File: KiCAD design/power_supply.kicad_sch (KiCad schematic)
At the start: 0 parts

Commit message: finished conectors / sensors / converters
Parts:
- added C? (x2): 1uF, Capacitor_SMD:C_0603_1608Metric_Pad1.08x0.95mm_HandSolder, symbol Device:C_Small
- added C?: 10uF, Capacitor_SMD:C_0603_1608Metric_Pad1.08x0.95mm_HandSolder, symbol Device:C_Small
- added C?: 22uF, Capacitor_SMD:C_0603_1608Metric_Pad1.08x0.95mm_HandSolder, symbol Device:C_Small
- added SW?: ~, composants_projet_footprint:1A11-NF5STSE-B, symbol Switch:SW_SPDT
- added U?: MIC5317, Package_TO_SOT_SMD:SOT-23-5, symbol Regulator_Linear:MCP1802x-xx02xOT
- added U?: A71117CH2-5.0TRG1, Package_TO_SOT_SMD:SOT-223-3_TabPin2, symbol Regulator_Linear:MCP1804x-1802xDB
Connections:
- new net +3V3: C?.1, U?.5 (VOUT)
- new net +5V: C?.1, C?.1, U?.1 (OUT), U?.1 (VIN), U?.3 (~{SHDN})
- new net +7.2V: C?.1, SW?.1 (A), U?.3 (IN)
- new net +BATT: SW?.2 (B)
- new net GND: C?.2, C?.2, C?.2, C?.2, U?.2 (GND), U?.2 (GND)
- no-connect marks 0 -> 1
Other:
- note added: "3.3V Power supply"
- note added: "5V Power supply"
- note added: "Bypass capacitor as close to the LDO (pin 1 VIN) as possible"
- note added: "SWITCH"
- company: (none) -> Oulu University
- title: (none) -> Power Supply

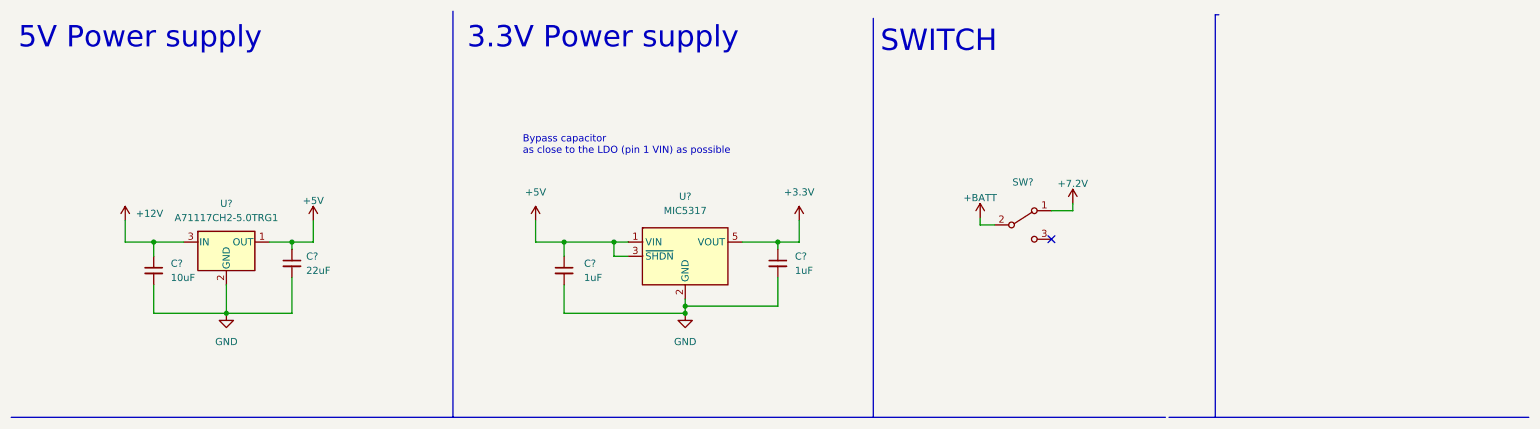
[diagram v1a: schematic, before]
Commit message: labeling and add of components. STM32 pin selected
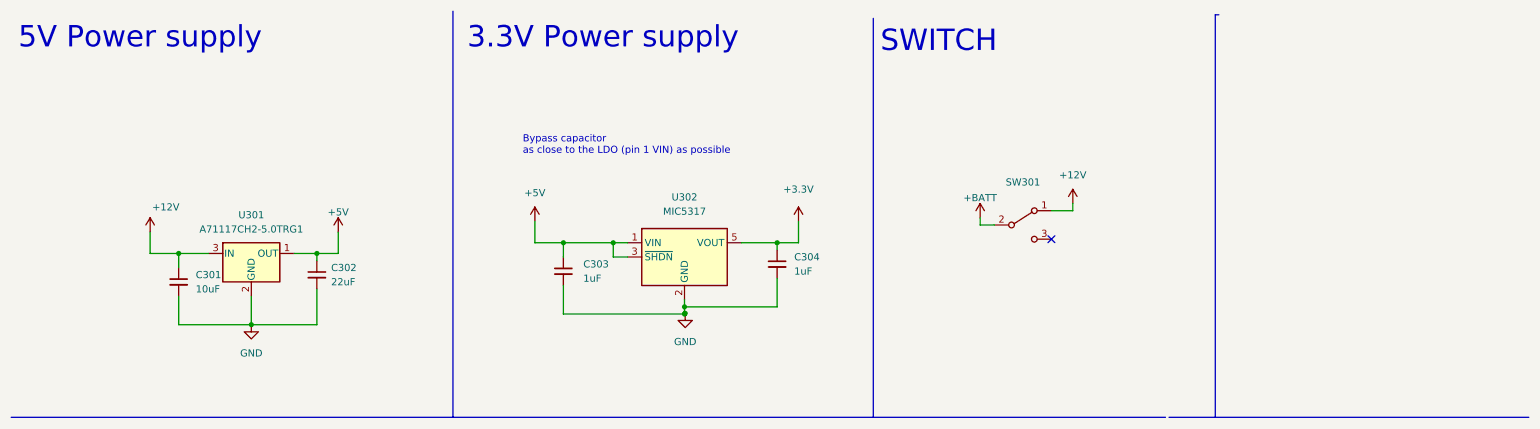
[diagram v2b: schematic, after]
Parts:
- gave numbers to parts that had none: 7
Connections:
- net +3V3 renamed +3.3V
- net +7.2V renamed +12V
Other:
- moved on the sheet: C301, C302, U301

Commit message: correction of errors
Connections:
- net +12V: no longer SW301.1 (A)
- net +BATT renamed BATT
- new net IP+: SW301.1 (A)
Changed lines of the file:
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@@
     (effects (font (size 3.81 3.81)) (justify left bottom))
+  )
+  (hierarchical_label "BATT" (shape input) (at 186.055 49.53 90)
+    (effects (font (size 1.27 1.27) bold) (justify left))
+  )
+  (hierarchical_label "IP+" (shape passive) (at 202.565 46.99 90)
+    (effects (font (size 1.27 1.27) bold) (justify left))
   )
   (symbol (lib_id "power:+5V") (at 71.628 52.07 0) (unit 1)
@@
   )
   (symbol (lib_id "power:+12V") (at 38.1 52.07 0) (unit 1)
-    (in_bom yes) (on_board yes)
+    (in_bom yes) (on_board yes) (fields_autoplaced)
     (property "Reference" "#PWR0105" (id 0) (at 38.1 55.88 0)
       (effects (font (size 1.27 1.27)) hide)
     )
-    (property "Value" "+12V" (id 1) (at 40.894 47.625 0))
+    (property "Value" "+12V" (id 1) (at 38.1 46.355 0))
     (property "Footprint" "" (id 2) (at 38.1 52.07 0)
       (effects (font (size 1.27 1.27)) hide)
@@
     (pin "1")
     (pin "2")
-  )
-  (symbol (lib_name "+3.3V_1") (lib_id "power:+3.3V") (at 153.67 50.165 0) (unit 1)
-    (in_bom yes) (on_board yes) (fields_autoplaced)
-    (property "Reference" "#PWR0104" (id 0) (at 153.67 53.975 0)
-      (effects (font (size 1.27 1.27)) hide)
-    )
-    (property "Value" "+3.3V" (id 1) (at 153.67 44.45 0))
-    (property "Footprint" "" (id 2) (at 153.67 50.165 0)
-      (effects (font (size 1.27 1.27)) hide)
-    )
-    (property "Datasheet" "" (id 3) (at 153.67 50.165 0)
-      (effects (font (size 1.27 1.27)) hide)
-    )
-    (pin "1")
   )
   (symbol (lib_id "Device:C_Small") (at 43.18 60.96 0) (unit 1)
@@
     (pin "2")
   )
-  (symbol (lib_id "power:+12V") (at 202.565 46.99 0) (unit 1)
-    (in_bom yes) (on_board yes) (fields_autoplaced)
-    (property "Reference" "#PWR0103" (id 0) (at 202.565 50.8 0)
-      (effects (font (size 1.27 1.27)) hide)
-    )
-    (property "Value" "+12V" (id 1) (at 202.565 41.91 0))
-    (property "Footprint" "" (id 2) (at 202.565 46.99 0)
-      (effects (font (size 1.27 1.27)) hide)
-    )
-    (property "Datasheet" "" (id 3) (at 202.565 46.99 0)
-      (effects (font (size 1.27 1.27)) hide)
-    )
-    (pin "1")
-  )
   (symbol (lib_id "Regulator_Linear:MCP1802x-xx02xOT") (at 133.35 56.515 0) (unit 1)
     (in_bom yes) (on_board yes) (fields_autoplaced)
@@
     (pin "3")
   )
-  (symbol (lib_id "power:+BATT") (at 186.055 49.53 0) (unit 1)
+  (symbol (lib_id "power:+3.3V") (at 153.67 50.165 0) (unit 1)
     (in_bom yes) (on_board yes) (fields_autoplaced)
-    (property "Reference" "#PWR0307" (id 0) (at 186.055 53.34 0)
+    (property "Reference" "#PWR0104" (id 0) (at 153.67 53.975 0)
       (effects (font (size 1.27 1.27)) hide)
     )
-    (property "Value" "+BATT" (id 1) (at 186.055 45.974 0))
-    (property "Footprint" "" (id 2) (at 186.055 49.53 0)
+    (property "Value" "+3.3V" (id 1) (at 153.67 44.45 0))
+    (property "Footprint" "" (id 2) (at 153.67 50.165 0)
       (effects (font (size 1.27 1.27)) hide)
     )
-    (property "Datasheet" "" (id 3) (at 186.055 49.53 0)
+    (property "Datasheet" "" (id 3) (at 153.67 50.165 0)
       (effects (font (size 1.27 1.27)) hide)
     )

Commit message: add purchase location (field PurchaseLoc) and price (field Price) to some main components, adding rest later
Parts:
- U301: Price (none) -> 0.94; PurchaseLoc (none) -> https://www.digikey.fi/en/products/detail/microchip-technol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
- U302: Price (none) -> 0.71; PurchaseLoc (none) -> https://www.digikey.fi/en/products/detail/microchip-technol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
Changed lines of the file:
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@@
+      (effects (font (size 1.27 1.27)) hide)
+    )
+    (property "PurchaseLoc" "https://www.digikey.fi/en/products/detail/microchip-technology/MCP1802T-3302I-OT/1679144" (id 4) (at 133.35 56.515 0)
+      (effects (font (size 1.27 1.27)) hide)
+    )
+    (property "Price" "0.71" (id 5) (at 133.35 56.515 0)
       (effects (font (size 1.27 1.27)) hide)
     )
@@
       (effects (font (size 1.27 1.27)) hide)
     )
+    (property "PurchaseLoc" "https://www.digikey.fi/en/products/detail/microchip-technology/MCP1804T-5002I-DB/2171415?s=N4IgTCBcDaILIGEAKBGAHABgCwBUC0ArBhmAJID0AIgEIgC6AvkA" (id 4) (at 56.134 55.88 0)
+      (effects (font (size 1.27 1.27)) hide)
+    )
+    (property "Price" "0.94" (id 5) (at 56.134 55.88 0)
+      (effects (font (size 1.27 1.27)) hide)
+    )

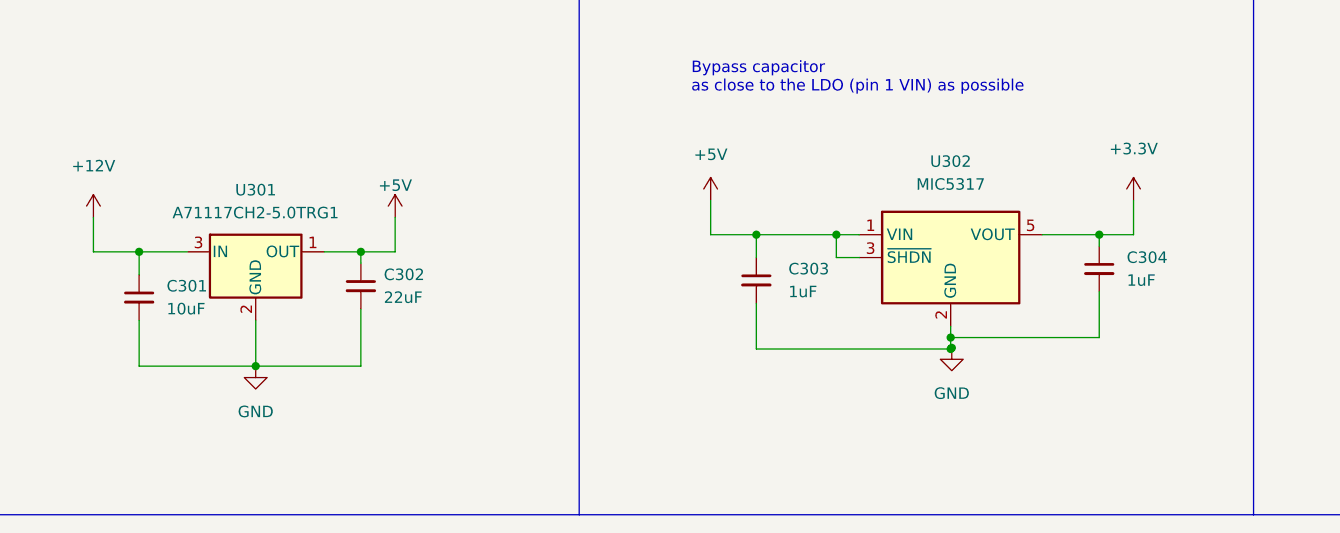
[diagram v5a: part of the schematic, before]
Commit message: Added capacitors and resistors
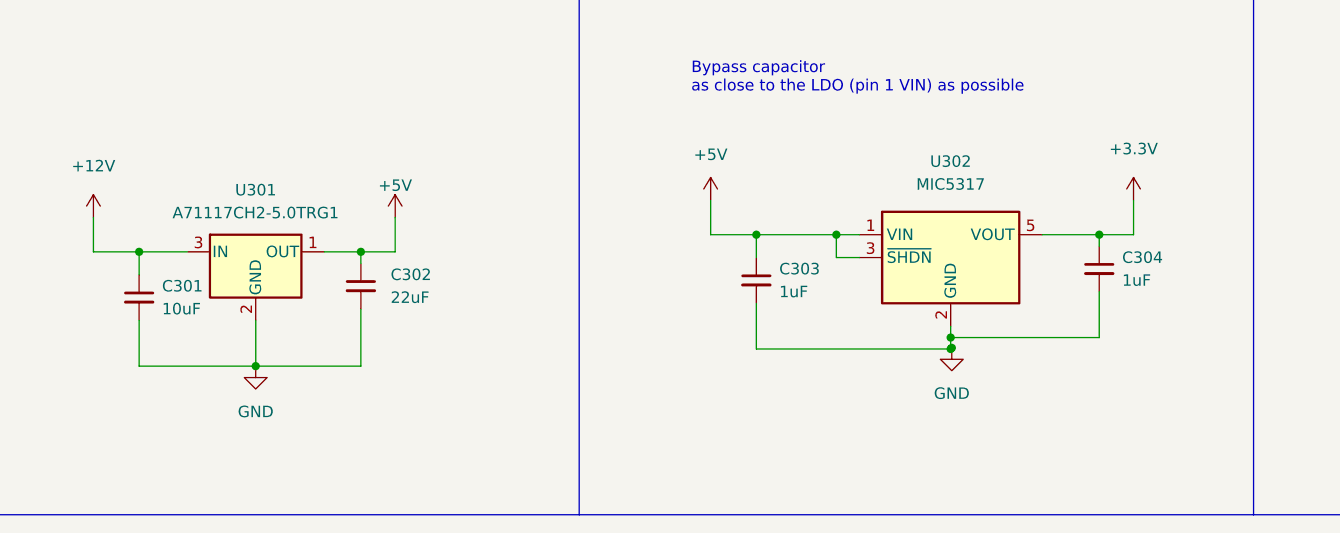
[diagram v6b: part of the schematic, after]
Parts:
- C301: footprint Capacitor_SMD:C_0603_1608Metric_Pad1.08x0.95mm_HandSolder -> Capacitor_SMD:C_0805_2012Metric; Price (none) -> 0,29; PurchaseLoc (none) -> https://www.digikey.fi/fi/products/detail/yageo/CC0805KKX5R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
- C302: footprint Capacitor_SMD:C_0603_1608Metric_Pad1.08x0.95mm_HandSolder -> Capacitor_SMD:C_0805_2012Metric; Price (none) -> 0,09; PurchaseLoc (none) -> https://www.digikey.fi/fi/products/detail/yageo/CC0805JRNPO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
- C303, C304: footprint Capacitor_SMD:C_0603_1608Metric_Pad1.08x0.95mm_HandSolder -> Capacitor_SMD:C_0805_2012Metric; Price (none) -> 0,13; PurchaseLoc (none) -> https://www.digikey.fi/fi/products/detail/yageo/CC0805KKX7R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
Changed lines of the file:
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@@
   (symbol (lib_id "Device:C_Small") (at 111.76 59.055 0) (unit 1)
     (in_bom yes) (on_board yes) (fields_autoplaced)
-    (property "Reference" "C303" (id 0) (at 115.316 57.7912 0)
+    (property "Reference" "C303" (id 0) (at 114.3 57.7912 0)
       (effects (font (size 1.27 1.27)) (justify left))
     )
-    (property "Value" "1uF" (id 1) (at 115.316 60.3312 0)
+    (property "Value" "1uF" (id 1) (at 114.3 60.3312 0)
       (effects (font (size 1.27 1.27)) (justify left))
     )
-    (property "Footprint" "Capacitor_SMD:C_0603_1608Metric_Pad1.08x0.95mm_HandSolder" (id 2) (at 111.76 59.055 0)
+    (property "Footprint" "Capacitor_SMD:C_0805_2012Metric" (id 2) (at 111.76 59.055 0)
       (effects (font (size 1.27 1.27)) hide)
     )
-    (property "Datasheet" "~" (id 3) (at 111.76 59.055 0)
+    (property "Datasheet" "https://www.yageo.com/upload/media/product/productsearch/datasheet/mlcc/UPY-GPHC_X7R_6.3V-to-250V_22.pdf" (id 3) (at 111.76 59.055 0)
+      (effects (font (size 1.27 1.27)) hide)
+    )
+    (property "PurchaseLoc" "https://www.digikey.fi/fi/products/detail/yageo/CC0805KKX7R7BB105/2103103" (id 4) (at 111.76 59.055 0)
+      (effects (font (size 1.27 1.27)) hide)
+    )
+    (property "Price" "0,13" (id 5) (at 111.76 59.055 0)
       (effects (font (size 1.27 1.27)) hide)
     )
@@
   (symbol (lib_id "Device:C_Small") (at 43.18 60.96 0) (unit 1)
     (in_bom yes) (on_board yes) (fields_autoplaced)
-    (property "Reference" "C301" (id 0) (at 46.228 59.6962 0)
+    (property "Reference" "C301" (id 0) (at 45.72 59.6962 0)
       (effects (font (size 1.27 1.27)) (justify left))
     )
-    (property "Value" "10uF" (id 1) (at 46.228 62.2362 0)
+    (property "Value" "10uF" (id 1) (at 45.72 62.2362 0)
       (effects (font (size 1.27 1.27)) (justify left))
     )
-    (property "Footprint" "Capacitor_SMD:C_0603_1608Metric_Pad1.08x0.95mm_HandSolder" (id 2) (at 43.18 60.96 0)
+    (property "Footprint" "Capacitor_SMD:C_0805_2012Metric" (id 2) (at 43.18 60.96 0)
       (effects (font (size 1.27 1.27)) hide)
     )
-    (property "Datasheet" "~" (id 3) (at 43.18 60.96 0)
+    (property "Datasheet" "https://www.yageo.com/upload/media/product/productsearch/datasheet/mlcc/UPY-GPHC_X5R_4V-to-50V_26.pdf" (id 3) (at 43.18 60.96 0)
+      (effects (font (size 1.27 1.27)) hide)
+    )
+    (property "PurchaseLoc" "https://www.digikey.fi/fi/products/detail/yageo/CC0805KKX5R8BB106/5195275" (id 4) (at 43.18 60.96 0)
+      (effects (font (size 1.27 1.27)) hide)
+    )
+    (property "Price" "0,29" (id 5) (at 43.18 60.96 0)
       (effects (font (size 1.27 1.27)) hide)
     )
@@
   (symbol (lib_id "Device:C_Small") (at 149.86 57.785 0) (unit 1)
     (in_bom yes) (on_board yes) (fields_autoplaced)
-    (property "Reference" "C304" (id 0) (at 152.908 56.5212 0)
+    (property "Reference" "C304" (id 0) (at 152.4 56.5212 0)
       (effects (font (size 1.27 1.27)) (justify left))
     )
-    (property "Value" "1uF" (id 1) (at 152.908 59.0612 0)
+    (property "Value" "1uF" (id 1) (at 152.4 59.0612 0)
       (effects (font (size 1.27 1.27)) (justify left))
     )
-    (property "Footprint" "Capacitor_SMD:C_0603_1608Metric_Pad1.08x0.95mm_HandSolder" (id 2) (at 149.86 57.785 0)
+    (property "Footprint" "Capacitor_SMD:C_0805_2012Metric" (id 2) (at 149.86 57.785 0)
       (effects (font (size 1.27 1.27)) hide)
     )
-    (property "Datasheet" "~" (id 3) (at 149.86 57.785 0)
+    (property "Datasheet" "https://www.yageo.com/upload/media/product/productsearch/datasheet/mlcc/UPY-GPHC_X7R_6.3V-to-250V_22.pdf" (id 3) (at 149.86 57.785 0)
+      (effects (font (size 1.27 1.27)) hide)
+    )
+    (property "PurchaseLoc" "https://www.digikey.fi/fi/products/detail/yageo/CC0805KKX7R7BB105/2103103" (id 4) (at 149.86 57.785 0)
+      (effects (font (size 1.27 1.27)) hide)
+    )
+    (property "Price" "0,13" (id 5) (at 149.86 57.785 0)
       (effects (font (size 1.27 1.27)) hide)
     )
@@
   (symbol (lib_id "Device:C_Small") (at 67.818 59.69 0) (unit 1)
     (in_bom yes) (on_board yes) (fields_autoplaced)
-    (property "Reference" "C302" (id 0) (at 70.358 58.4262 0)
+    (property "Reference" "C302" (id 0) (at 71.12 58.4262 0)
       (effects (font (size 1.27 1.27)) (justify left))
     )
-    (property "Value" "22uF" (id 1) (at 70.358 60.9662 0)
+    (property "Value" "22uF" (id 1) (at 71.12 60.9662 0)
       (effects (font (size 1.27 1.27)) (justify left))
     )
-    (property "Footprint" "Capacitor_SMD:C_0603_1608Metric_Pad1.08x0.95mm_HandSolder" (id 2) (at 67.818 59.69 0)
+    (property "Footprint" "Capacitor_SMD:C_0805_2012Metric" (id 2) (at 67.818 59.69 0)
       (effects (font (size 1.27 1.27)) hide)
     )
-    (property "Datasheet" "~" (id 3) (at 67.818 59.69 0)
+    (property "Datasheet" "https://www.yageo.com/upload/media/product/productsearch/datasheet/mlcc/UPY-GP_NP0_16V-to-50V_18.pdf" (id 3) (at 67.818 59.69 0)
       (effects (font (size 1.27 1.27)) hide)
     )
+    (property "PurchaseLoc" "https://www.digikey.fi/fi/products/detail/yageo/CC0805JRNPO9BN220/302837" (id 4) (at 67.818 59.69 0)
+      (effects (font (size 1.27 1.27)) hide)
+    )
+    (property "Price" "0,09" (id 5) (at 67.818 59.69 0)
+      (effects (font (size 1.27 1.27)) hide)
+    )

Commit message: add link to switch and 1k resistor
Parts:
- SW301: Price (none) -> 1.05; PurchaseLoc (none) -> https://www.digikey.com/en/products/detail/e-switch/RR511D1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
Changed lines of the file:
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@@
+      (effects (font (size 1.27 1.27)) hide)
+    )
+    (property "Price" "1.05" (id 4) (at 193.675 50.8 0)
+      (effects (font (size 1.27 1.27)) hide)
+    )
+    (property "PurchaseLoc" "https://www.digikey.com/en/products/detail/e-switch/RR511D1121/2116256" (id 5) (at 193.675 50.8 0)
       (effects (font (size 1.27 1.27)) hide)
     )

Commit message: use . as decimal separator
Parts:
- C301: Price 0,29 -> 0.29
- C302: Price 0,09 -> 0.09
- C303, C304: Price 0,13 -> 0.13
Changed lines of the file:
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@@
       (effects (font (size 1.27 1.27)) hide)
     )
-    (property "Price" "0,13" (id 5) (at 111.76 59.055 0)
+    (property "Price" "0.13" (id 5) (at 111.76 59.055 0)
       (effects (font (size 1.27 1.27)) hide)
     )
@@
       (effects (font (size 1.27 1.27)) hide)
     )
-    (property "Price" "0,29" (id 5) (at 43.18 60.96 0)
+    (property "Price" "0.29" (id 5) (at 43.18 60.96 0)
       (effects (font (size 1.27 1.27)) hide)
     )
@@
       (effects (font (size 1.27 1.27)) hide)
     )
-    (property "Price" "0,13" (id 5) (at 149.86 57.785 0)
+    (property "Price" "0.13" (id 5) (at 149.86 57.785 0)
       (effects (font (size 1.27 1.27)) hide)
     )
@@
       (effects (font (size 1.27 1.27)) hide)
     )
-    (property "Price" "0,09" (id 5) (at 67.818 59.69 0)
+    (property "Price" "0.09" (id 5) (at 67.818 59.69 0)
       (effects (font (size 1.27 1.27)) hide)
     )
